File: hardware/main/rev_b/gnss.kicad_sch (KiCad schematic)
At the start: 22 parts, among them J30 GNSS_UFL, Q30 2N7002, U30 LG77LICMD

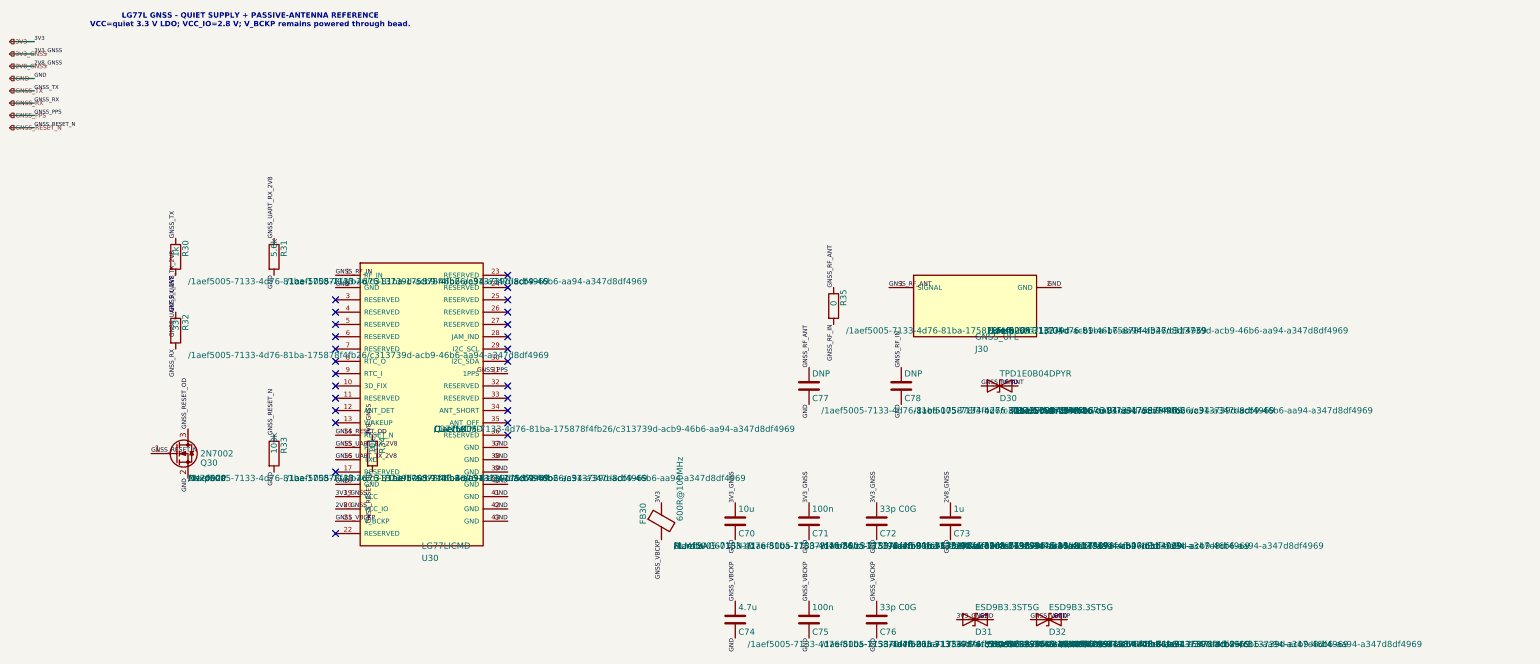
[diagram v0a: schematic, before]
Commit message: build: route and validate rev-b boards
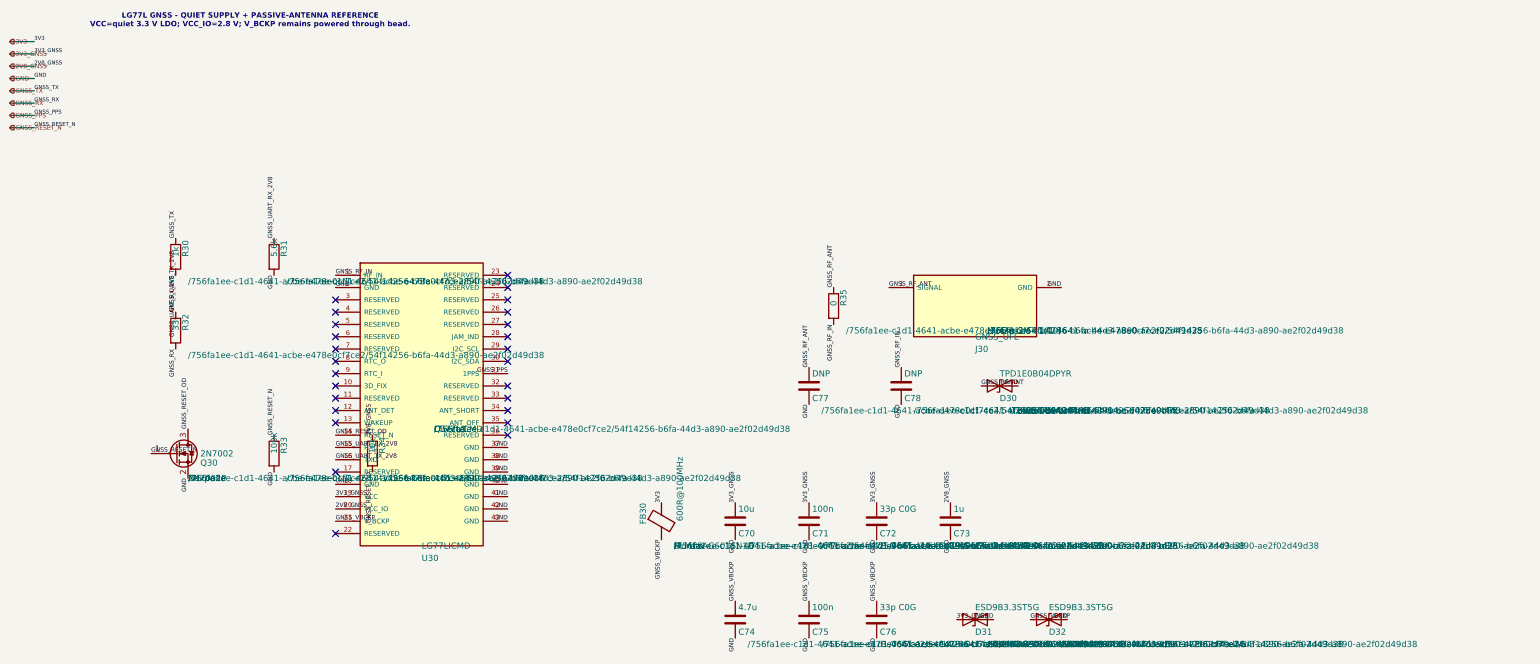
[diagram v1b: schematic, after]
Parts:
- C70, C71, C72, C73, C74, C75, C76, C77, C78, D30, D31, D32, FB30, J30, Q30, R30, R31, R32, R33, R34, R35, U30: hierarchy_path /1aef5005-7133-4d76-81ba-175878f4fb26/c313739d-acb9-46b6-aa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 -> /756fa1ee-c1d1-4641-acbe-e478e0cf7ce2/54f14256-b6fa-44d3-a8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

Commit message: build: route and validate rev-b boards
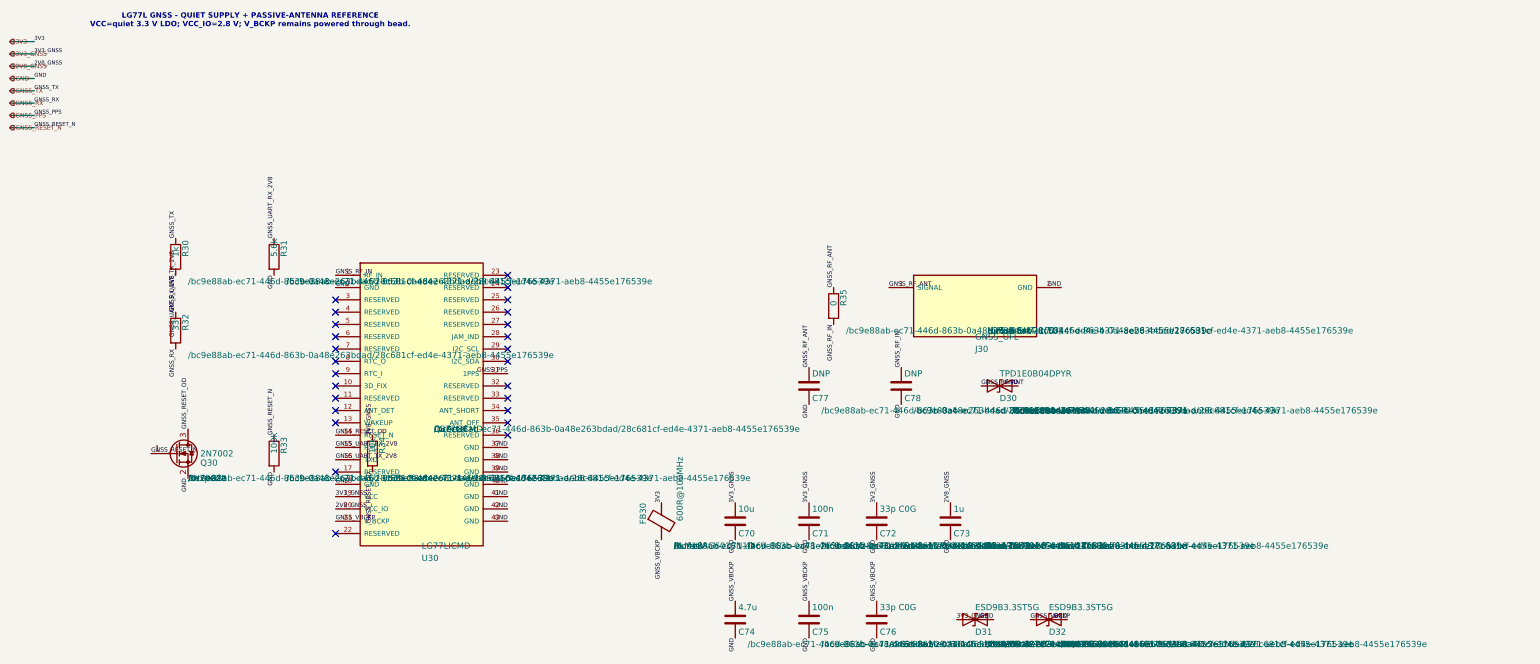
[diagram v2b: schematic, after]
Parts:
- C70, C71, C72, C73, C74, C75, C76, C77, C78, D30, D31, D32, FB30, J30, Q30, R30, R31, R32, R33, R34, R35, U30: hierarchy_path /756fa1ee-c1d1-4641-acbe-e478e0cf7ce2/54f14256-b6fa-44d3-a8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 -> /bc9e88ab-ec71-446d-863b-0a48e263bdad/28c681cf-ed4e-4371-ae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

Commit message: build: route and validate rev-b boards
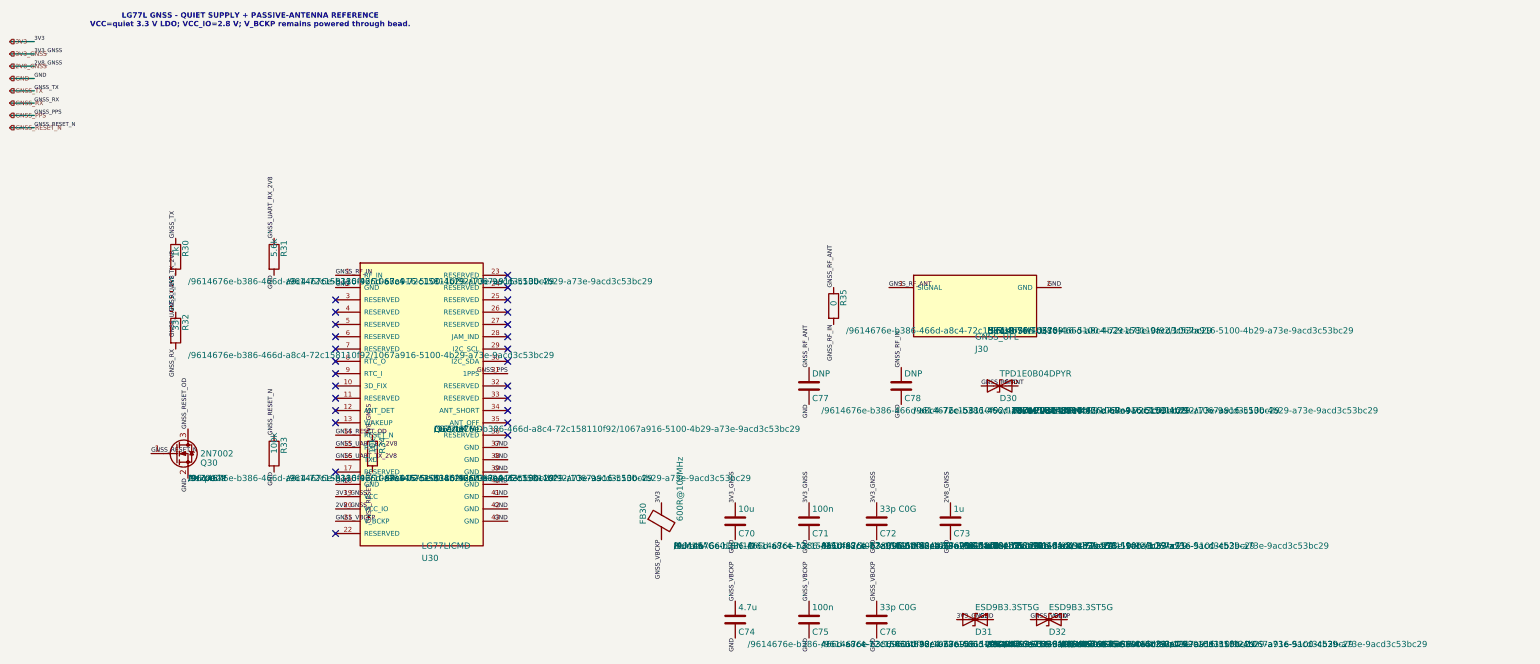
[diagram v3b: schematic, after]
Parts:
- C70, C71, C72, C73, C74, C75, C76, C77, C78, D30, D31, D32, FB30, J30, Q30, R30, R31, R32, R33, R34, R35, U30: hierarchy_path /bc9e88ab-ec71-446d-863b-0a48e263bdad/28c681cf-ed4e-4371-ae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 -> /9614676e-b386-466d-a8c4-72c158110f92/1067a916-5100-4b29-a7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
